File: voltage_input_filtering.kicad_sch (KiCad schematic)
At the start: 0 parts

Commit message: Launchpad controller revision 06/03/2024
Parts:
- added C93: 100n, symbol Device:C
- added D1: SD36_SOD323, Diode_SMD:D_SOD-323, symbol Diode:SD36_SOD323
- added F4: Polyfuse, symbol Device:Polyfuse
- added J27: Conn_01x04_Socket, symbol Connector:Conn_01x04_Socket
- added R69: 1k, symbol Device:R
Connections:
- net Vout: now also C93.1, R69.2
- new net: D1.2 (A2), J27.2 (Pin_2), R69.1
- new net: F4.1, J27.1 (Pin_1)
- new net +12L: F4.2
- new net GND: C93.2, D1.1 (A1), J27.4 (Pin_4)
- no-connect marks 1 -> 2
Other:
- note added: "Cutoff frequency of 1.5915 kHz Bidirectional TVS Diode with clamp voltage of 36V. Maybe switch to 24V clamp."
- note added: "Not gonna do open-wire detection. Left it as a NC to make it easier to add later though"
- note added: "Would remove the connector from this sheet. Move to root sheet. Nah fuck that Unless someone else wants to..."

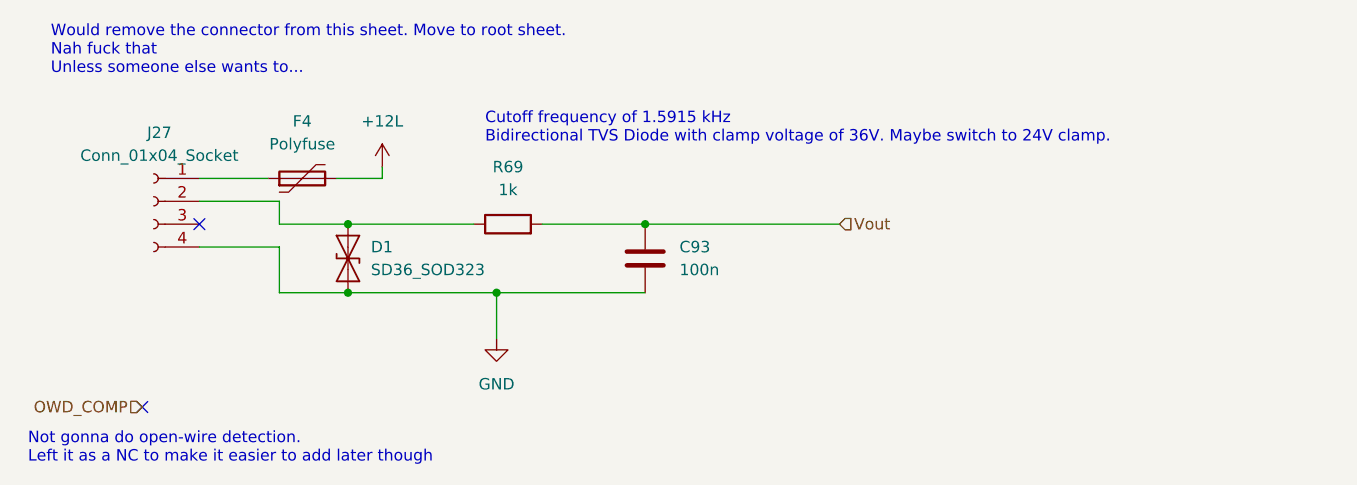
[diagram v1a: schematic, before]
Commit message: added footprints to almost all components
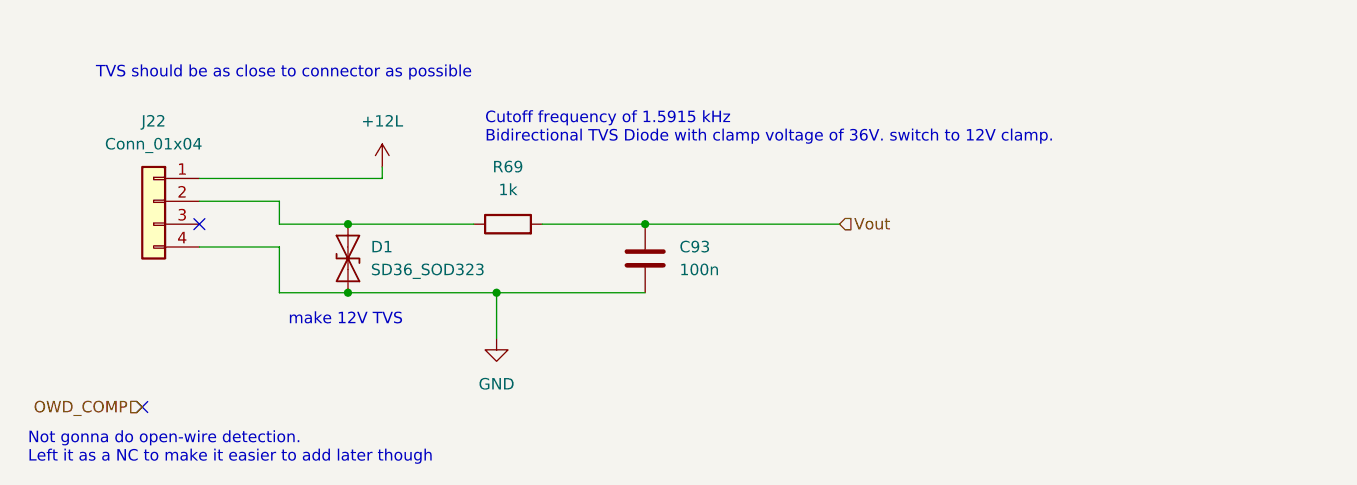
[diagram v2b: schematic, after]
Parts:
- removed F4: Polyfuse, symbol Device:Polyfuse
- removed J27: Conn_01x04_Socket, symbol Connector:Conn_01x04_Socket
- added J22: Conn_01x04, Connector_JST:JST_GH_BM04B-GHS-TBT_1x04-1MP_P1.25mm_Vertical, symbol Connector_Generic:Conn_01x04
- C93: footprint (none) -> Capacitor_SMD:C_0603_1608Metric_Pad1.08x0.95mm_HandSolder
- D1: footprint Diode_SMD:D_SOD-323 -> Diode_SMD:D_SOD-323_HandSoldering; Mouser# (none) -> 576-SD36C-01FTG
- R69: footprint (none) -> Resistor_SMD:R_0805_2012Metric_Pad1.20x1.40mm_HandSolder
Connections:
- net +12L: now also J22.1 (Pin_1)
- net GND: now also J22.4 (Pin_4)
- net at D1.2 (A2), R69.1: now also J22.2 (Pin_2)
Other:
- note added: "Cutoff frequency of 1.5915 kHz Bidirectional TVS Diode with clamp voltage of 36V. switch to 12V clamp."
- note added: "TVS should be as close to connector as possible"
- note added: "make 12V TVS"
- note removed: "Cutoff frequency of 1.5915 kHz Bidirectional TVS Diode with clamp voltage of 36V. Maybe switch to 24V clamp."
- note removed: "Would remove the connector from this sheet. Move to root sheet. Nah fuck that Unless someone else wants to..."
